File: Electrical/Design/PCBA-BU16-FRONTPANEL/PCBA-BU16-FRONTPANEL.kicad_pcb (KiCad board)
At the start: 2 copper layers, 104.4 x 104.4 mm, 0 parts

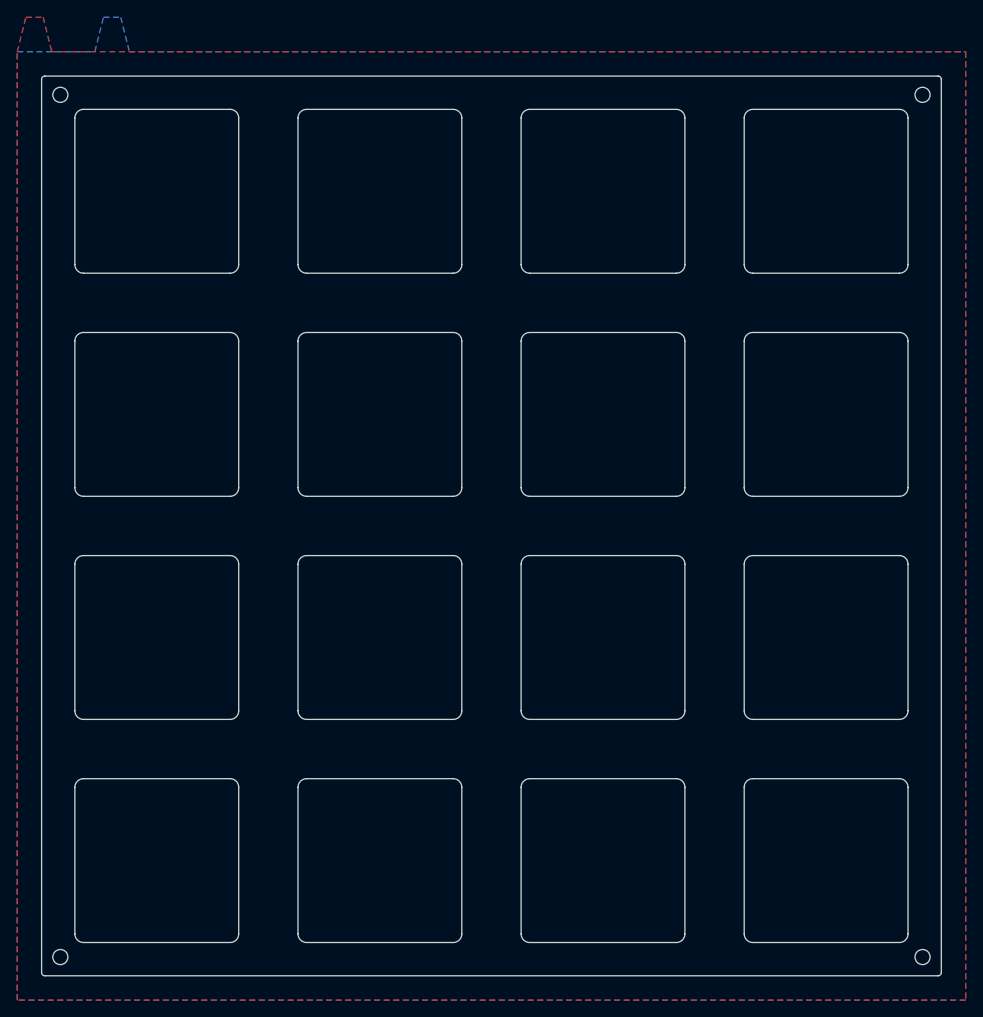
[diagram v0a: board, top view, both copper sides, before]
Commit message: SUKU all pcb frontpanels updated to use proper footprints, silkscreen variables and design rules
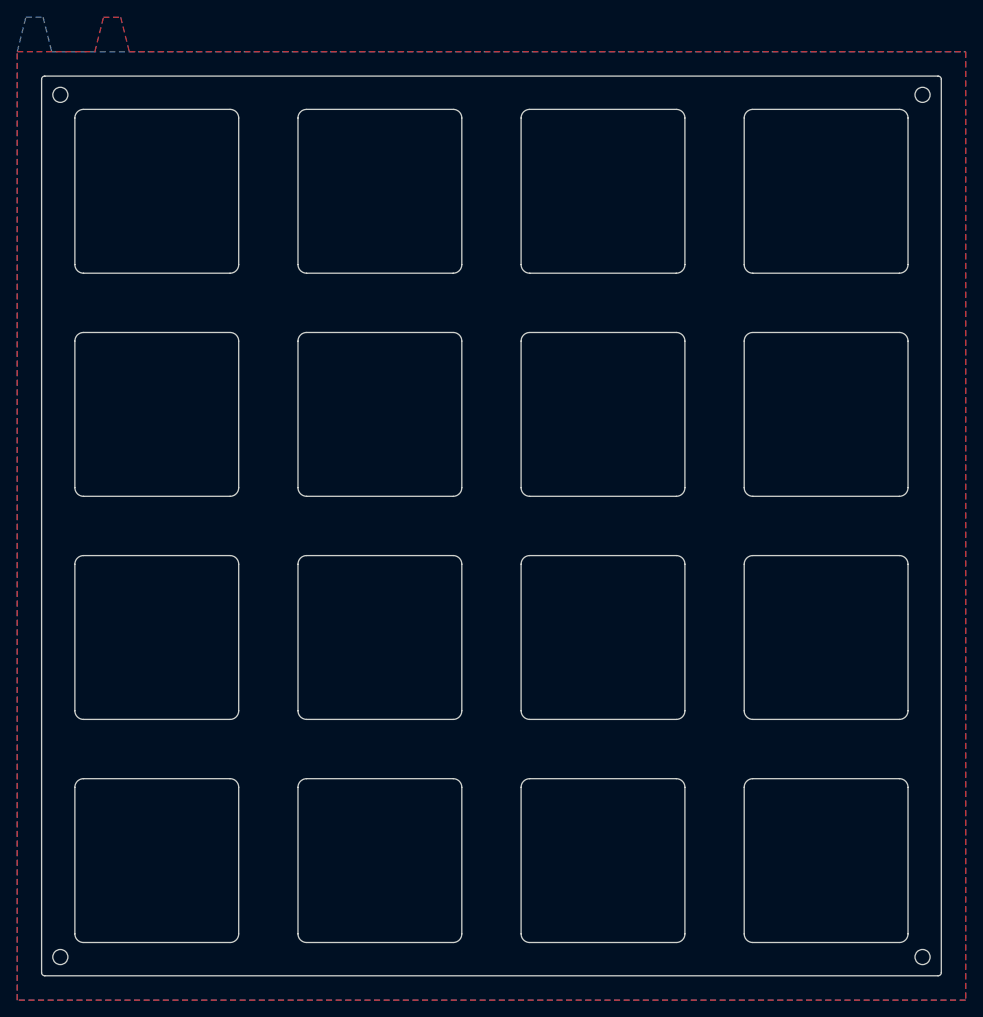
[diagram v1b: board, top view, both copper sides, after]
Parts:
- added H505: Button, suku_basics:FP_BUTTON, F.Cu at (61.2, 61.2)
- added H506: Button, suku_basics:FP_BUTTON, F.Cu at (61.2, 87.1)
- added H507: Button, suku_basics:FP_BUTTON, F.Cu at (61.2, 112.9)
- added H508: Button, suku_basics:FP_BUTTON, F.Cu at (61.2, 138.8)
- added H513: Button, suku_basics:FP_BUTTON, F.Cu at (87.1, 61.2)
- added H514: Button, suku_basics:FP_BUTTON, F.Cu at (87.1, 87.1)
- added H515: Button, suku_basics:FP_BUTTON, F.Cu at (87.1, 112.9)
- added H516: Button, suku_basics:FP_BUTTON, F.Cu at (87.1, 138.8)
- added H521: Button, suku_basics:FP_BUTTON, F.Cu at (112.9, 61.2)
- added H522: Button, suku_basics:FP_BUTTON, F.Cu at (112.9, 87.1)
- added H523: Button, suku_basics:FP_BUTTON, F.Cu at (112.9, 112.9)
- added H524: Button, suku_basics:FP_BUTTON, F.Cu at (112.9, 138.8)
- added H529: Button, suku_basics:FP_BUTTON, F.Cu at (138.8, 61.2)
- added H530: Button, suku_basics:FP_BUTTON, F.Cu at (138.8, 87.1)
- added H531: Button, suku_basics:FP_BUTTON, F.Cu at (138.8, 112.9)
- added H532: Button, suku_basics:FP_BUTTON, F.Cu at (138.8, 138.8)
- added H533: Outline, suku_basics:FP_OUTLINE, F.Cu at (100.0, 100.0)
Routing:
- added copper zone on B.Cu, net (none)
- added copper zone on F.Cu, net (none)
- removed copper zone on B.Cu, net GND
- removed copper zone on F.Cu, net GND
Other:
- outline, holes or cut-outs redrawn
- board text added: "${PROJECTNAME} ${HASH} ${DATE}"
